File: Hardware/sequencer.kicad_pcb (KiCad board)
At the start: 2 copper layers, 157.5 x 116 mm, 100 parts, among them IC1 74HC165N, IC2 74HC165N, IC3 74HC165N, IC4 74HC165N, J1 SJ-3523-SMT-TR, U1 Teensy3.6

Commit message: PCB rev 1.2
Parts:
- added REF**: MountingHole_3.2mm_M3_ISO7380_Pad, Mounting_Holes:MountingHole_3.2mm_M3_ISO7380_Pad, F.Cu at (220.2, 38.9)
- added REF**: MountingHole_3.2mm_M3_ISO7380_Pad, Mounting_Holes:MountingHole_3.2mm_M3_ISO7380_Pad, F.Cu at (71.8, 38.9)
- moved C1 16.9 mm to (214.3, 39.2), turned to 270 degrees
- moved C2 15.0 mm to (211.3, 39.2), turned to 270 degrees
- moved J1 10.8 mm to (219.7, 49.6), turned to 180 degrees
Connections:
- J1 pad 2: /Audio1 -> /Audio2
- J1 pad 3: /Audio2 -> /Audio1
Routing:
- net /AudioGND: track 43.2 -> 80.4 mm
- net Net-(C2-Pad1): track 109.4 -> 78.6 mm
- net Net-(C1-Pad1): track 115.8 -> 86.0 mm
- net /Audio2: track 17.7 -> 5.70 mm
- net /Audio1: track 10.8 -> 14.8 mm
- net /JOY_B: track 76.3 -> 73.8 mm
- net /JOY_A: track 72.5 -> 74.3 mm
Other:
- board text added: "POLARON PCB rev1.2 (c) 2018 TOM ZUEBLIN github.com/zueblin/Polaron"
- board text removed: "v1.1 2018 TOM ZUEBLIN"

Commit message: rotated pot 1 / 2 footprint by 180 degrees
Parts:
- moved RV2 14.9 mm to (202.5, 79.2), turned to 90 degrees
- moved RV1 14.9 mm to (219.0, 79.2), turned to 90 degrees
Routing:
- net /JOY_B: track 73.8 -> 87.4 mm
- net /JOY_A: track 74.3 -> 86.5 mm

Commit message: rev 1.3 pcb - Pots rotated by 180 degrees - Added circuit for trigger input
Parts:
- added D31: 1N4148, Diodes_THT:D_DO-35_SOD27_P2.54mm_Vertical_AnodeUp, B.Cu at (73.1, 55.4)
- added J2: SJ-3523-SMT-TR, SJ-3523-SMT-TR:CUI_SJ-3523-SMT-TR, F.Cu at (71.7, 48.4)
- added Q1: 2N3904, TO_SOT_Packages_THT:TO-92_Inline_Wide, B.Cu at (80.7, 41.5)
- added R31: 10k, Resistors_SMD:R_1206_HandSoldering, B.Cu at (78.0, 55.4)
- added R32: 10k, Resistors_SMD:R_1206_HandSoldering, F.Cu at (77.5, 38.9)
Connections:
- U1 pad 30: (no net) -> /Trigger-Input
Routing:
- net /Trigger-Input: track 0.00 -> 42.0 mm
- net VCC: track 310.0 -> 285.4 mm
- net Net-(D31-Pad1): track 0.00 -> 21.3 mm
- net Net-(J2-Pad2): track 0.00 -> 7.46 mm, vias 0 -> 1
- net GND: track 144.2 -> 147.8 mm
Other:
- board text added: "POLARON PCB rev1.3 (c) 2019 TOM ZUEBLIN github.com/zueblin/Polaron"
- board text removed: "POLARON PCB rev1.2 (c) 2018 TOM ZUEBLIN github.com/zueblin/Polaron"

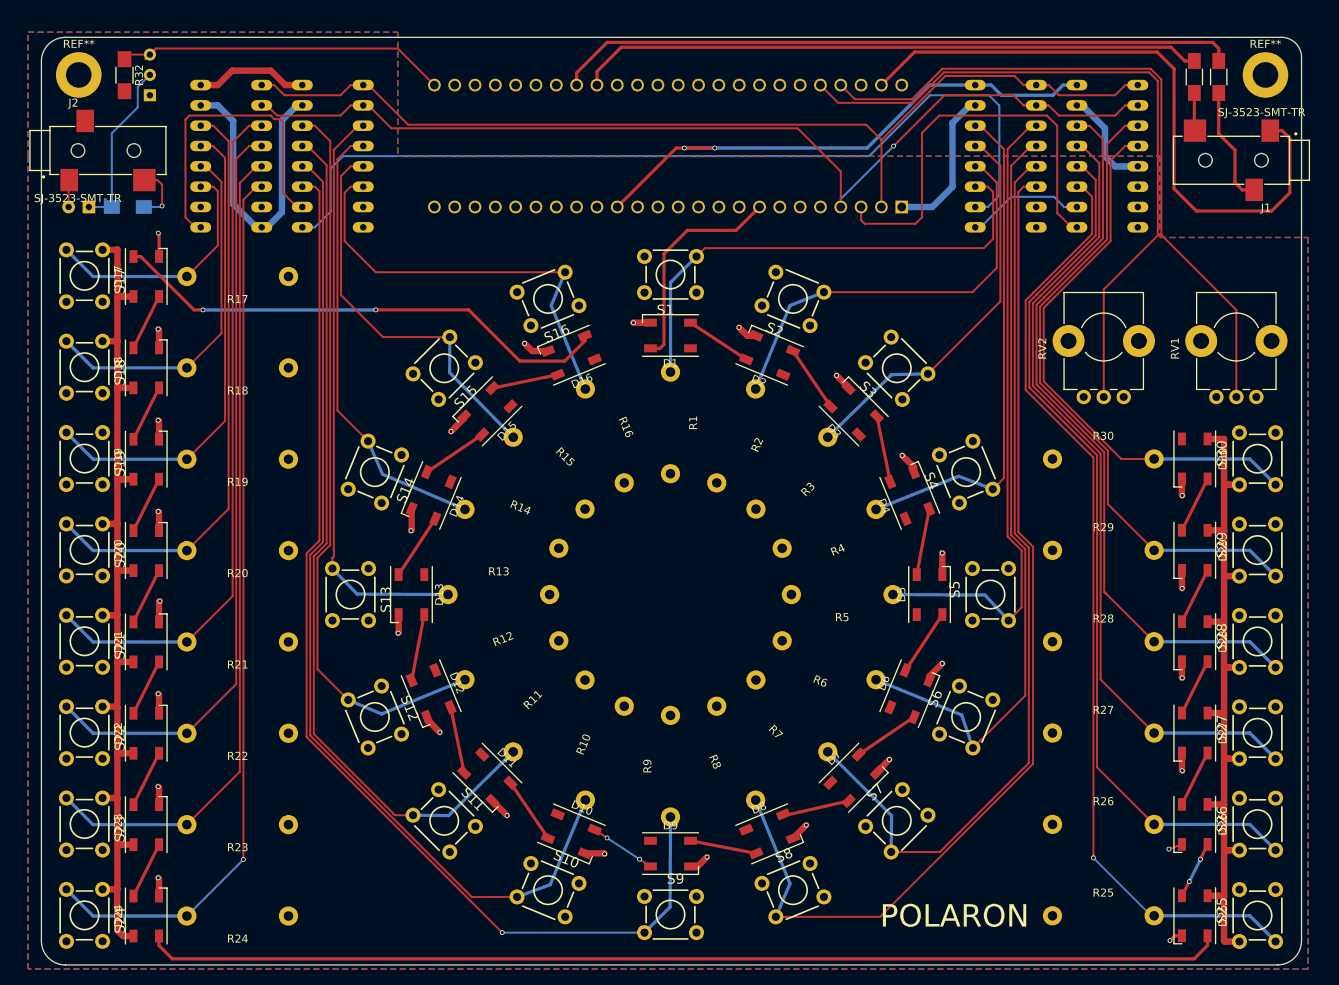
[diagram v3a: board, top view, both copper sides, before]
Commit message: Hardware Rev 1.4: Function buttons and track buttons now use SMD Resistors, so that there is space on the PCB for text labels for each function button
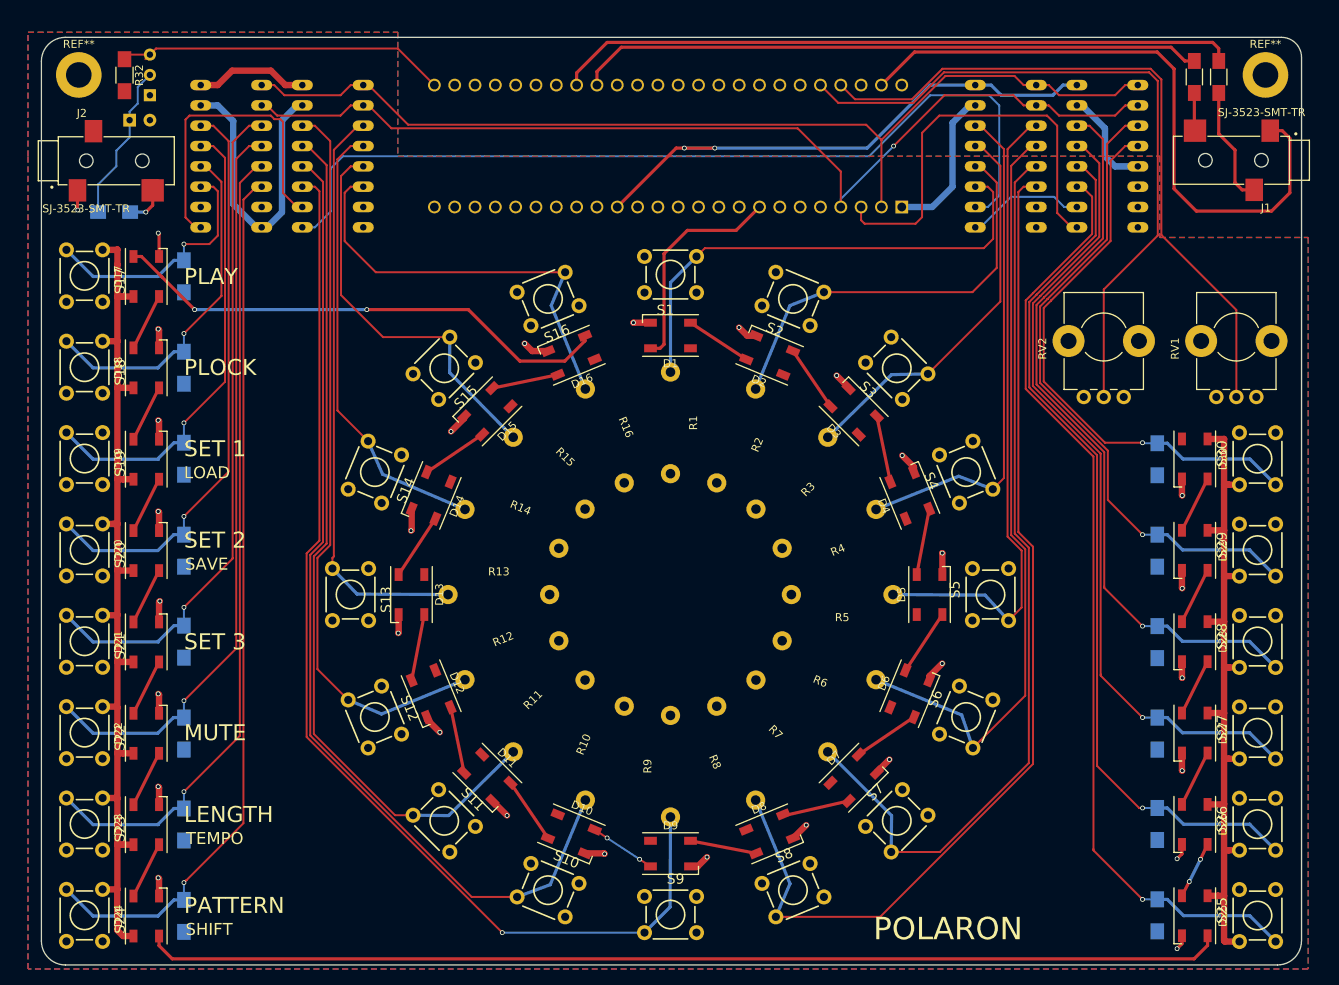
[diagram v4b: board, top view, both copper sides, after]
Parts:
- R17, R18, R19, R20, R21, R22, R23, R24, R25, R26, R27, R28, R29, R30: footprint modules:R_Axial_DIN0411_L9.9mm_D3.6mm_P12.70mm_Horizontal_noSilkscreen -> Resistors_SMD:R_1206_HandSoldering; moved to B.Cu
- moved R27 13.1 mm to (206.6, 121.2), turned to 90 degrees
- moved R26 13.1 mm to (206.6, 132.5), turned to 90 degrees
- moved R28 13.1 mm to (206.6, 109.8), turned to 90 degrees
- moved R25 13.1 mm to (206.6, 144.0), turned to 90 degrees
- moved R29 13.1 mm to (206.6, 98.4), turned to 90 degrees
- moved R30 13.1 mm to (206.6, 87.0), turned to 90 degrees
- moved R19 13.1 mm to (85.0, 86.9), turned to 90 degrees
- moved R21 13.1 mm to (85.0, 109.7), turned to 90 degrees
- moved R22 13.1 mm to (85.0, 121.2), turned to 90 degrees
- moved R23 13.1 mm to (85.0, 132.6), turned to 90 degrees
- moved R17 13.1 mm to (85.0, 64.1), turned to 90 degrees
- moved R24 13.1 mm to (85.0, 144.0), turned to 90 degrees
- moved R20 13.1 mm to (85.0, 98.4), turned to 90 degrees
- moved R18 13.1 mm to (85.0, 75.5), turned to 90 degrees
- moved D31 12.0 mm to (78.2, 44.6), turned to 0 degrees
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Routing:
- net Net-(D31-Pad1): track 21.3 -> 19.8 mm
- net Net-(IC1-Pad12): track 44.9 -> 43.5 mm, vias 0 -> 1
- net Net-(IC1-Pad14): track 74.1 -> 72.7 mm, vias 0 -> 1
- net Net-(IC1-Pad5): track 103.0 -> 101.6 mm, vias 0 -> 1
- net Net-(IC1-Pad6): track 111.9 -> 110.5 mm
- net Net-(IC1-Pad3): track 85.8 -> 84.4 mm, vias 0 -> 1
- net Net-(IC1-Pad13): track 59.7 -> 58.4 mm, vias 0 -> 1
- net Net-(IC1-Pad4): track 94.6 -> 93.3 mm, vias 0 -> 1
- net Net-(J2-Pad2): track 7.46 -> 8.52 mm
- net Net-(IC4-Pad11): track 119.5 -> 118.6 mm
- net GND: track 147.8 -> 147.1 mm, vias 30 -> 31
- net Net-(IC4-Pad14): track 93.9 -> 93.2 mm, vias 0 -> 1
- net Net-(IC1-Pad11): track 31.1 -> 31.6 mm, vias 0 -> 1
- net Net-(IC4-Pad13): track 101.2 -> 100.9 mm, vias 0 -> 1
- net Net-(IC4-Pad3): track 82.1 -> 81.9 mm, vias 0 -> 1
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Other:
- board text added: "LENGTH"
- board text added: "LOAD"
- board text added: "MUTE"
- board text added: "PATTERN"
- board text added: "PLAY"
- board text added: "PLOCK"
- board text added: "POLARON PCB rev1.4 (c) 2019 TOM ZUEBLIN github.com/zueblin/Polaron"
- board text added: "SAVE"
- board text added: "SET 1"
- board text added: "SET 2"
- board text added: "SET 3"
- board text added: "SHIFT"
- board text added: "TEMPO"
- board text removed: "POLARON PCB rev1.3 (c) 2019 TOM ZUEBLIN github.com/zueblin/Polaron"
